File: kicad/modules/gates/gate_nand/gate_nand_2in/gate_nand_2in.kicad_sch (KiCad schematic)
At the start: 4 parts

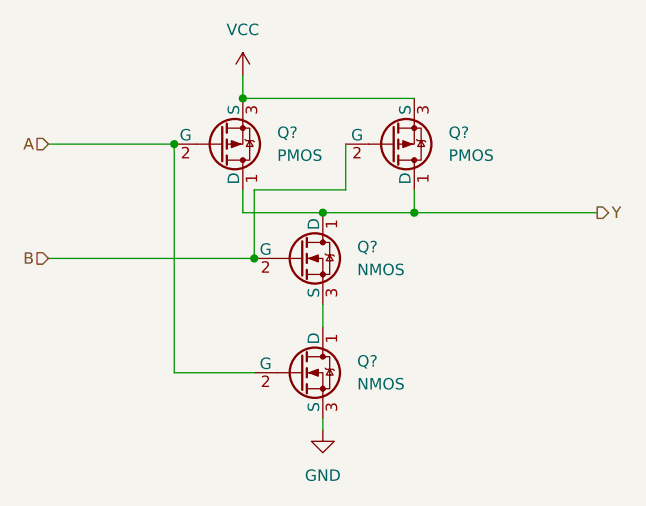
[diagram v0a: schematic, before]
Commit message: feat: complete circuit designs for all ALU components
* Designed all gate modules: AND, OR, NOT, NAND, NOR, XOR (1-bit and 8-bit variants)

* Completed multiplexer hierarchy: 2:1, 4:1, and 8:1 8-bit muxes

* Finalized add_sub board schematic and LED panel designs

* Added new board modules: flags, main_control, main_logic

* Updated Logisim top-level ALU circuit

* Note: KiCad directory path errors to be resolved next (iCloud sync issue), then begin PCB routing
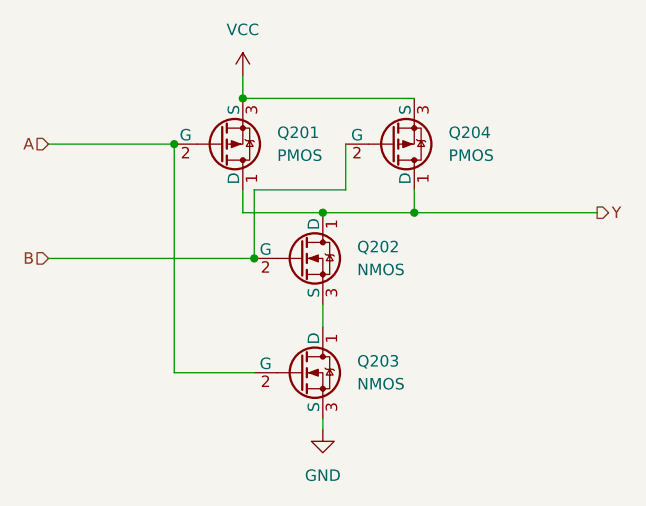
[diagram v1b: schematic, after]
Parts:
- gave numbers to parts that had none: 4

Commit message: Fix KiCad file paths and complete core circuit design
- Fixed file path errors across all KiCad schematics and projects
- Completed core circuit designs:
  * Adder and subtractor modules (adder2, adder8)
  * LED panels (led_panel_1) with display circuits
  * Flag LED circuits for status indicators
  * All dependent logic gate modules (AND, OR, NOT, NAND, NOR, XOR)
  * All multiplexer modules (2:1, 4:1, 8:1, 8-bit)
  * Main control board schematics
  * Flags board schematics
- Updated .gitignore to exclude KiCad backups, cache files, and lock files
- Ready for pin placement and routing of control buses, power rails, and inter-board signals
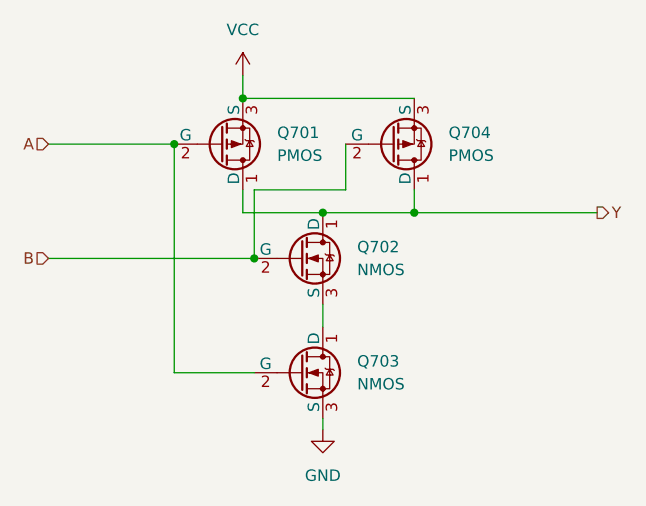
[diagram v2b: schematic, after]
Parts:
- renumbered Q201 to Q701, Q202 to Q702, Q203 to Q703, Q204 to Q704
